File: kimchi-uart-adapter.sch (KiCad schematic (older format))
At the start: 17 parts

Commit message: Completed schematics
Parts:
- added C? (x2): 1 uF, symbol Device:C_Small
- added D? (x2): LED, symbol Device:LED
- added J?: Conn_01x02, symbol Connector_Generic:Conn_01x02
- added R? (x2): 270 Ohm, symbol Device:R_Small_US
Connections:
- wire segments 62 -> 99
- no-connect marks 4 -> 9
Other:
- note added: "1v8 Voltage Regulator"
- note added: "JST Connector"
- note added: "RX LED"
- note added: "TX LED"
- moved on the sheet: IC?, J?, U?

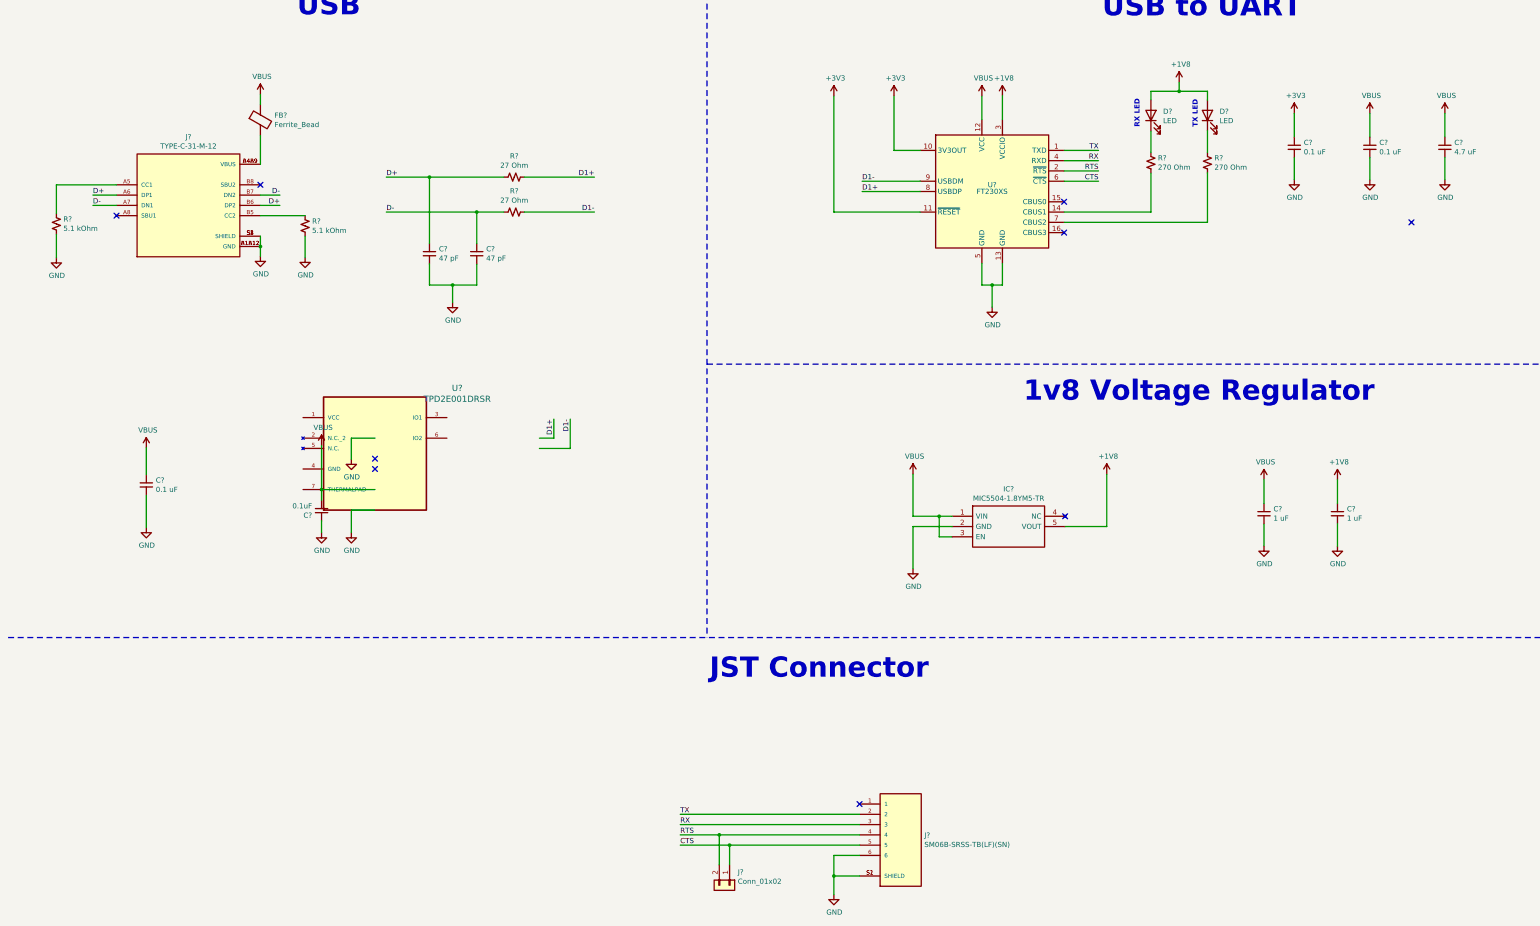
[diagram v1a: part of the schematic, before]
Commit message: Completed partial routing
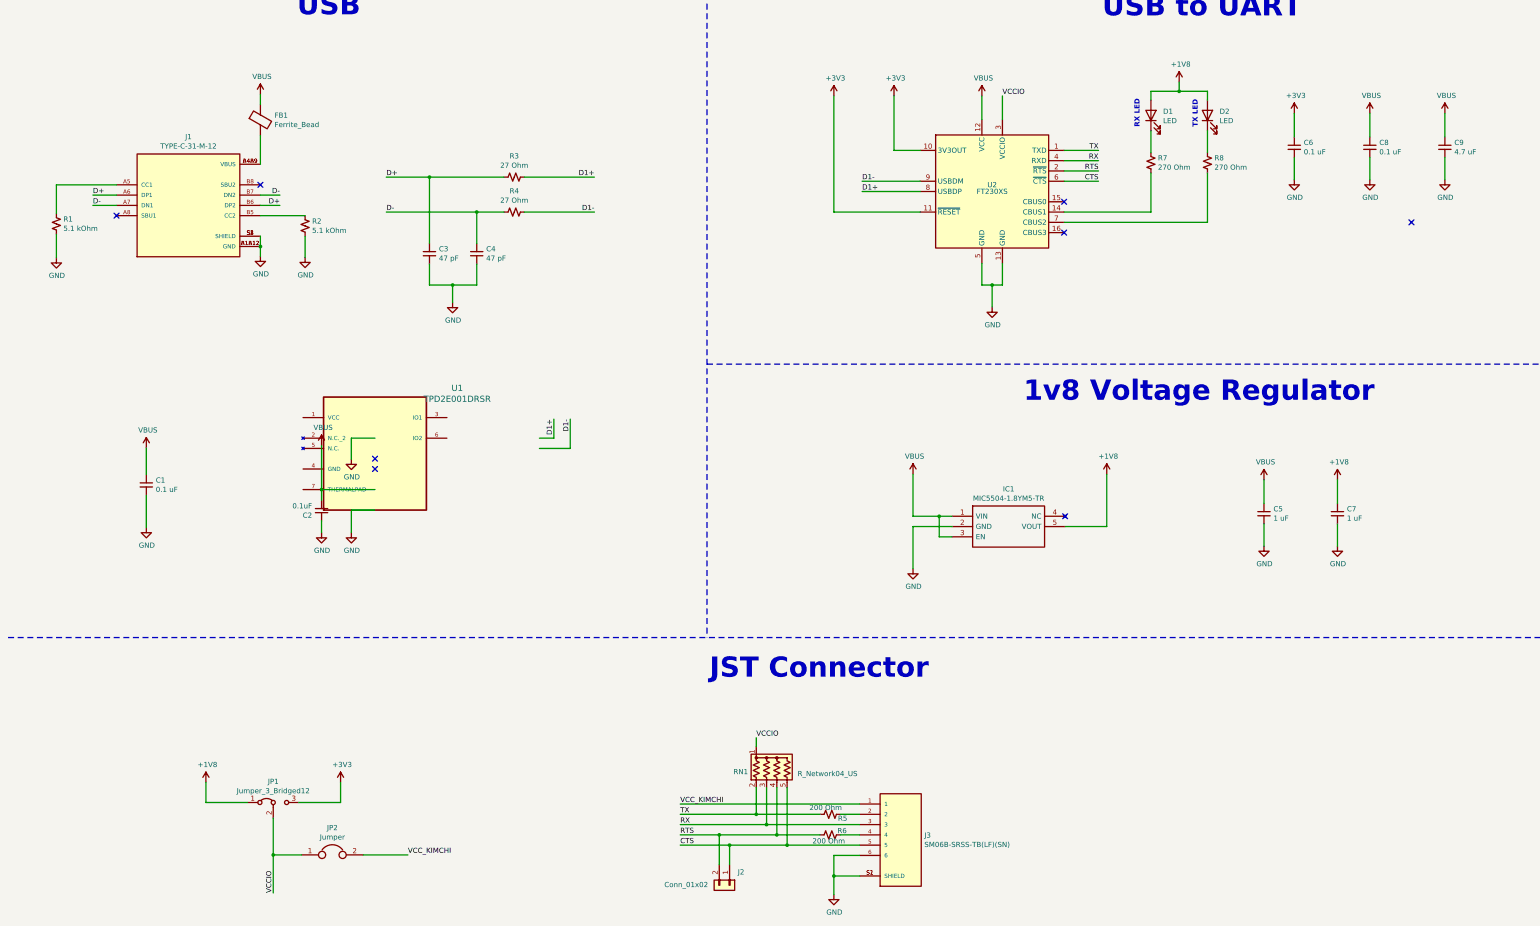
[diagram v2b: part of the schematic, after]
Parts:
- added JP1: Jumper_3_Bridged12, Jumper:SolderJumper-3_P1.3mm_Open_RoundedPad1.0x1.5mm_NumberLabels, symbol Jumper:Jumper_3_Bridged12
- added JP2: Jumper, Jumper:SolderJumper-2_P1.3mm_Open_RoundedPad1.0x1.5mm, symbol Device:Jumper
- added R5, R6: 200 Ohm, Resistor_SMD:R_0603_1608Metric, symbol Device:R_Small_US
- added RN1: R_Network04_US, Resistor_SMD:R_Array_Concave_4x0603, symbol Device:R_Network04_US
- C1, C2, C3, C4, C5, C6, C7, C8, C9: renamed from C?; footprint (none) -> Capacitor_SMD:C_0603_1608Metric
- D1, D2: renamed from D?; footprint (none) -> LED_SMD:LED_0603_1608Metric
- FB1: renamed from FB?; footprint (none) -> Resistor_SMD:R_0603_1608Metric
- IC1: renamed from IC?; footprint SOT95P280X130-5N -> MIC5504-1.8YM5-TR:SOT95P280X130-5N
- J1: renamed from J?; footprint HRO_TYPE-C-31-M-12 -> USB-TYPE-C:HRO_TYPE-C-31-M-12
- J2: renamed from J?; footprint (none) -> Connector_PinHeader_2.54mm:PinHeader_1x02_P2.54mm_Vertical_SMD_Pin1Left
- J3: renamed from J?; footprint JST_SM06B-SRSS-TB(LF)(SN) -> SM06B-SRSS-TB(LF)(SN):JST_SM06B-SRSS-TB(LF)(SN)
- R1, R2, R3, R4, R7, R8: renamed from R?; footprint (none) -> Resistor_SMD:R_0603_1608Metric
- U1: renamed from U?; footprint DRS6_1P9X1P2 -> footprints:TPD2E001DRSR
- gave numbers to parts that had none: 1
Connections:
- net labels added: VCCIO, VCC_KIMCHI
- wire segments 99 -> 119
- no-connect marks 9 -> 8

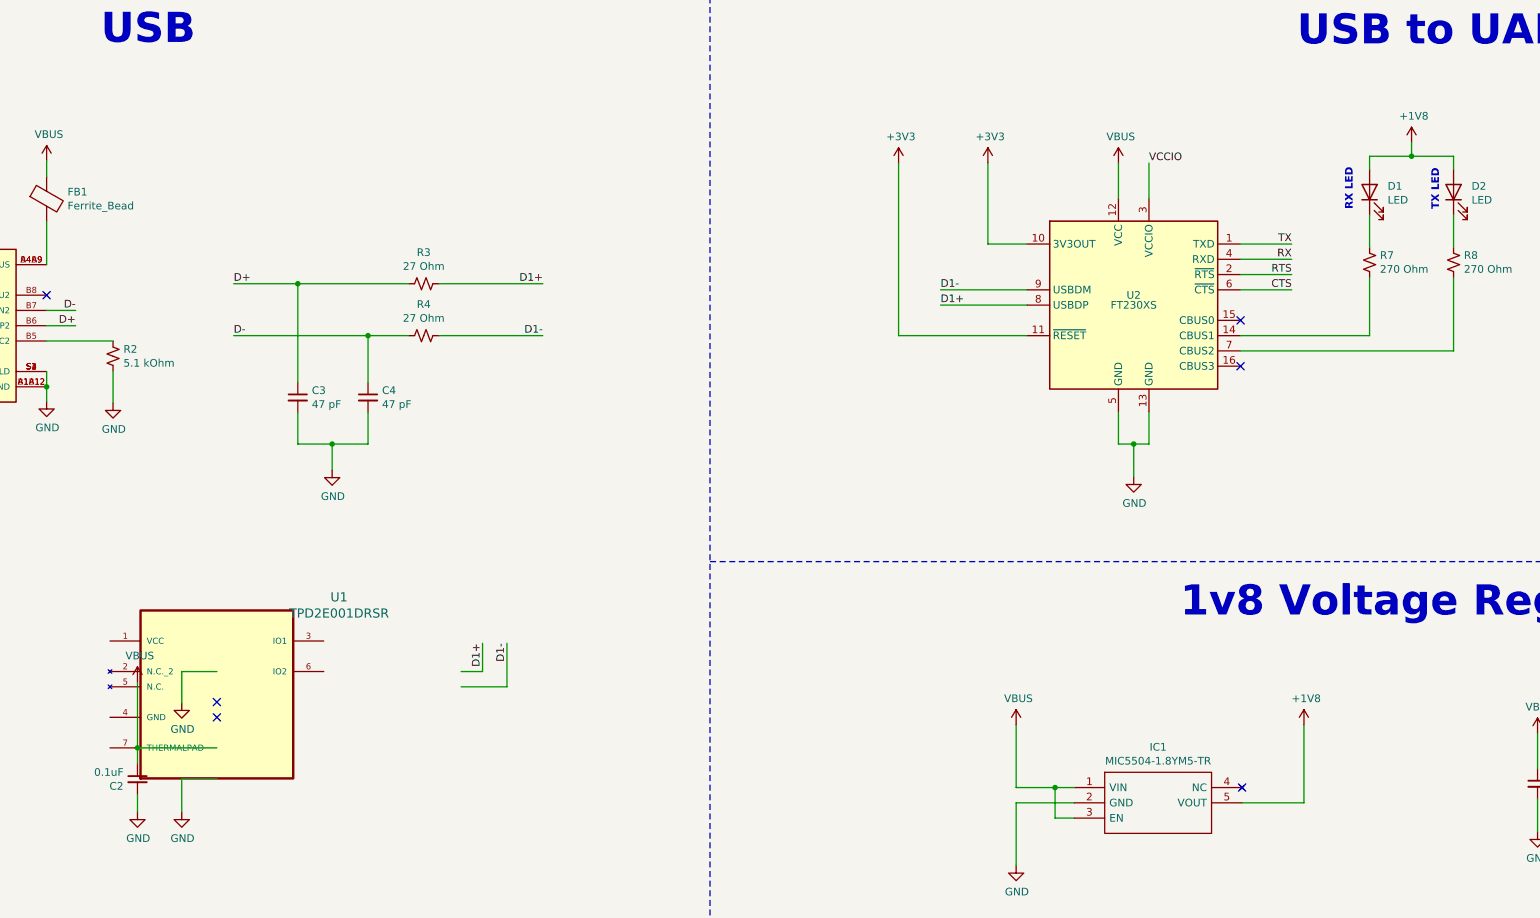
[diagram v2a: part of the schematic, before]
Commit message: Almost completed routing, waiting for fix to the resistor network issue. Also replaced model for TPD2E001 chip
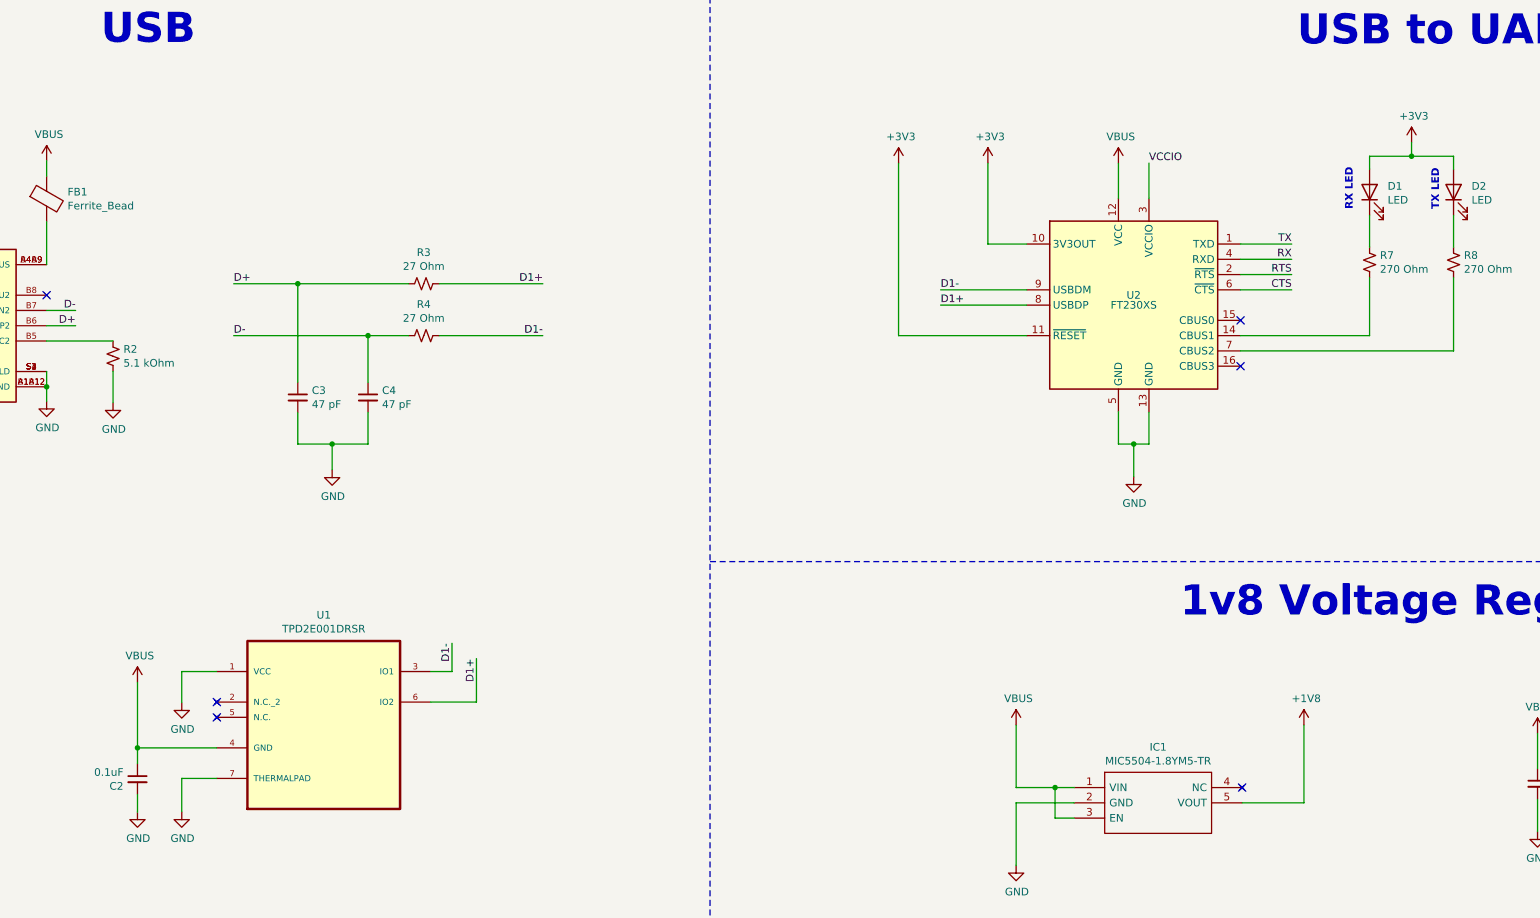
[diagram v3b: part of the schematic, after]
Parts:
- J2: footprint Connector_PinHeader_2.54mm:PinHeader_1x02_P2.54mm_Vertical_SMD_Pin1Left -> Connector_PinHeader_1.27mm:PinHeader_1x02_P1.27mm_Vertical
- U1: footprint footprints:TPD2E001DRSR -> footprints:SON95P315X315X80-7N; MPN (none) -> TPD2E001DRSR; OC_FARNELL (none) -> 1603426; OC_NEWARK (none) -> 54M7403; PACKAGE (none) -> SON-6; SUPPLIER (none) -> Texas Instruments
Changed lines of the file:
@@
 	2945 3065 2945 3160
 Connection ~ 2945 3065
-$Comp
-L TPD2E001DRSR:TPD2E001DRSR U1
-U 1 1 60BA2BA3
-P 4060 4930
-F 0 "U1" H 4860 5417 60  0000 C CNN
-F 1 "TPD2E001DRSR" H 4860 5311 60  0000 C CNN
-F 2 "footprints:TPD2E001DRSR" H 4860 5270 60  0001 C CNN
-F 3 "" H 4060 4930 60  0000 C CNN
-	1    4060 4930
-	1    0    0    -1
-$EndComp
 NoConn ~ 4060 5130
 NoConn ~ 4060 5230
@@
 $EndComp
 Wire Wire Line
-	5660 4930 5800 4930
-Wire Wire Line
-	5800 4930 5800 4745
-Wire Wire Line
-	5960 5030 5960 4745
-Wire Wire Line
-	5660 5030 5960 5030
-Text Label 5800 4745 3    50   ~ 0
+	5460 4930 5600 4930
+Wire Wire Line
+	5600 4930 5600 4745
+Wire Wire Line
+	5760 5130 5760 4845
+Wire Wire Line
+	5460 5130 5760 5130
+Text Label 5600 4745 3    50   ~ 0
+D1-
+Text Label 5760 4845 3    50   ~ 0
 D1+
-Text Label 5960 4745 3    50   ~ 0
-D1-
 Wire Wire Line
 	4060 5430 3540 5430
@@
 	1    12160 1790
 	0    -1   -1   0
-$EndComp
-$Comp
-L power:+1V8 #PWR022
-U 1 1 60C62824
-P 11885 1465
-F 0 "#PWR022" H 11885 1315 50  0001 C CNN
-F 1 "+1V8" H 11900 1638 50  0000 C CNN
-F 2 "" H 11885 1465 50  0001 C CNN
-F 3 "" H 11885 1465 50  0001 C CNN
-	1    11885 1465
-	1    0    0    -1
 $EndComp
 Wire Wire Line
@@
 F 0 "J2" V 7382 9360 50  0000 L CNN
 F 1 "Conn_01x02" V 7505 8645 50  0000 L CNN
-F 2 "Connector_PinHeader_2.54mm:PinHeader_1x02_P2.54mm_Vertical_SMD_Pin1Left" H 7510 9280 50  0001 C CNN
+F 2 "Connector_PinHeader_1.27mm:PinHeader_1x02_P1.27mm_Vertical" H 7510 9280 50  0001 C CNN
 F 3 "~" H 7510 9280 50  0001 C CNN
 	1    7510 9280
@@
 	1    0    0    -1
 $EndComp
+$Comp
+L power:+3V3 #PWR0101
+U 1 1 60CDFAD7
+P 11885 1465
+F 0 "#PWR0101" H 11885 1315 50  0001 C CNN
+F 1 "+3V3" H 11900 1638 50  0000 C CNN
+F 2 "" H 11885 1465 50  0001 C CNN
+F 3 "" H 11885 1465 50  0001 C CNN
+	1    11885 1465
+	1    0    0    -1
+$EndComp
+$Comp
+L TPD2E001DRSR:TPD2E001DRSR U1
+U 1 1 60D0D5BF
+P 4760 5130
+F 0 "U1" H 4760 5700 50  0000 C CNN
+F 1 "TPD2E001DRSR" H 4760 5609 50  0000 C CNN
+F 2 "footprints:SON95P315X315X80-7N" H 4760 5130 50  0001 L BNN
+F 3 "" H 4760 5130 50  0001 L BNN
+F 4 "SON-6" H 4760 5130 50  0001 L BNN "PACKAGE"
+F 5 "Texas Instruments" H 4760 5130 50  0001 L BNN "SUPPLIER"
+F 6 "1603426" H 4760 5130 50  0001 L BNN "OC_FARNELL"
+F 7 "54M7403" H 4760 5130 50  0001 L BNN "OC_NEWARK"
+F 8 "TPD2E001DRSR" H 4760 5130 50  0001 L BNN "MPN"
+	1    4760 5130
+	1    0    0    -1
+$EndComp

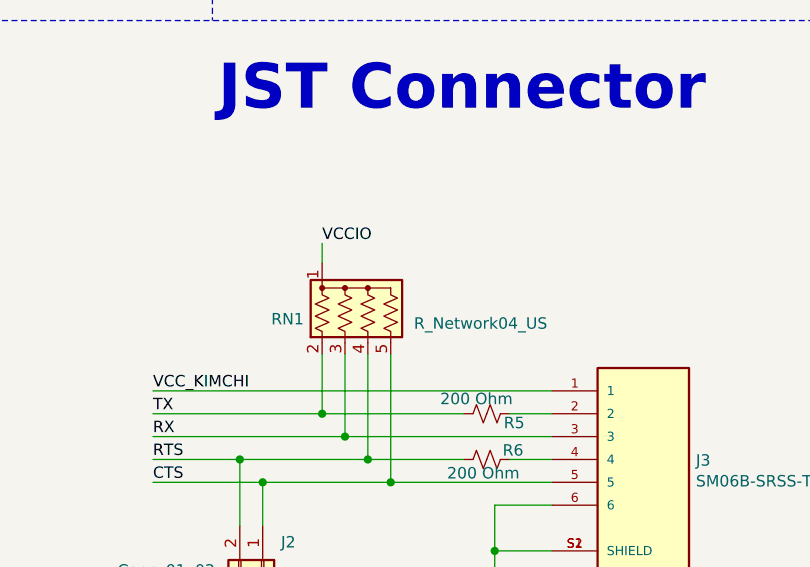
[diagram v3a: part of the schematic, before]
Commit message: Completed routing
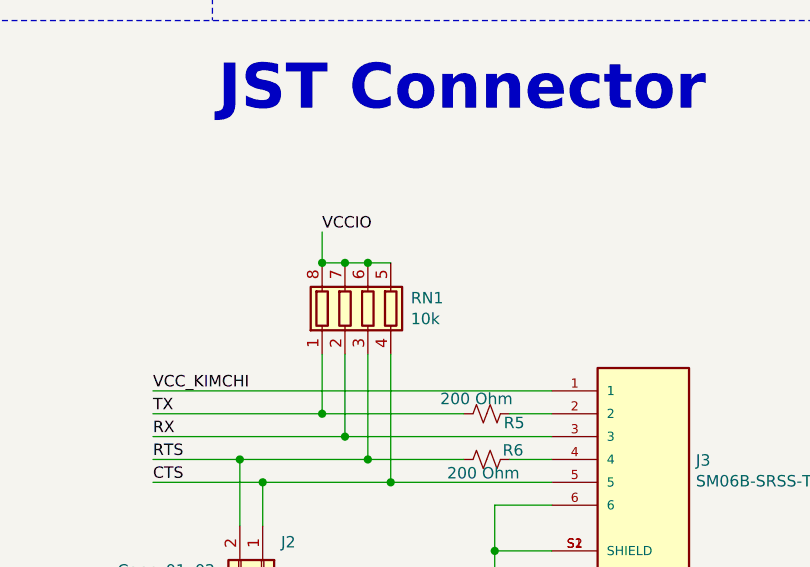
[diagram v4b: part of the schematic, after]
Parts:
- removed RN1: R_Network04_US, Resistor_SMD:R_Array_Concave_4x0603, symbol Device:R_Network04_US
- added RN1: 10k, Resistor_SMD:R_Array_Convex_4x0603, symbol Device:R_Pack04
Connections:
- net CTS: now also RN1.4 (R4.1)
- net RTS: now also RN1.3 (R3.1)
- net RX: now also RN1.2 (R2.1)
- net TX: now also RN1.1 (R1.1)
- net VCCIO: now also RN1.5 (R4.2), RN1.6 (R3.2), RN1.7 (R2.2), RN1.8 (R1.2)
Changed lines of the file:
@@
 	7510 8890 7030 8890
-$Comp
-L Device:R_Network04_US RN1
-U 1 1 60BCEC9D
-P 7970 8130
-F 0 "RN1" H 7690 8084 50  0000 R CNN
-F 1 "R_Network04_US" H 8755 8065 50  0000 R CNN
-F 2 "Resistor_SMD:R_Array_Concave_4x0603" V 8245 8130 50  0001 C CNN
-F 3 "http://www.vishay.com/docs/31509/csc.pdf" H 7970 8130 50  0001 C CNN
-	1    7970 8130
-	1    0    0    -1
-$EndComp
 $Comp
 L Device:R_Small_US R5
@@
 	8390 8790 7970 8790
 Connection ~ 7410 8790
-Wire Wire Line
-	7770 7930 7770 7845
-Text Label 7770 7845 0    50   ~ 0
+Text Label 7770 7795 0    50   ~ 0
 VCCIO
 Wire Wire Line
@@
 	1    0    0    -1
 $EndComp
+Wire Wire Line
+	7870 7930 7770 7930
+Connection ~ 7870 7930
+Wire Wire Line
+	7970 7930 7870 7930
+Wire Wire Line
+	8070 7930 7970 7930
+Connection ~ 7970 7930
+$Comp
+L Device:R_Pack04 RN1
+U 1 1 60D2B075
+P 7970 8130
+F 0 "RN1" H 8158 8176 50  0000 L CNN
+F 1 "10k" H 8158 8085 50  0000 L CNN
+F 2 "Resistor_SMD:R_Array_Convex_4x0603" V 8245 8130 50  0001 C CNN
+F 3 "~" H 7970 8130 50  0001 C CNN
+	1    7970 8130
+	1    0    0    -1
+$EndComp
+Wire Wire Line
+	7770 7795 7770 7930
+Connection ~ 7770 7930
 $EndSCHEMATC
